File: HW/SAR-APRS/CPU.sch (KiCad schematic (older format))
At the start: 16 parts

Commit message: schematic update
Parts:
- removed J?: USB_B_Micro, symbol Connector:USB_B_Micro
- added C? (x3): 100nF, symbol device:C_Small
- added D? (x2): LED, symbol device:LED
- added J?: USB_B_Mini, symbol Connector:USB_B_Mini
- added R? (x2): 680, symbol device:R_Small
- added R? (x2): 1k, symbol device:R_Small
- added Y?: 16MHz, symbol device:Crystal_Small
- C? (x5): value C_Small -> 100nF
- J?: value HEADER_2x03 -> JTAG
- R?: value R_Small -> 1k
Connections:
- net labels added: BAT_SENS, D11\MOSI, D12\MISO, D13\SCK, GPS_RXD, GPS_TXD, LED, RESET, RFMOD_AUX, RFMOD_PTT, RXD, TXD
- wire segments 72 -> 113
- no-connect marks 1 -> 12
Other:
- moved on the sheet: C?, D?, J?, R?, U?

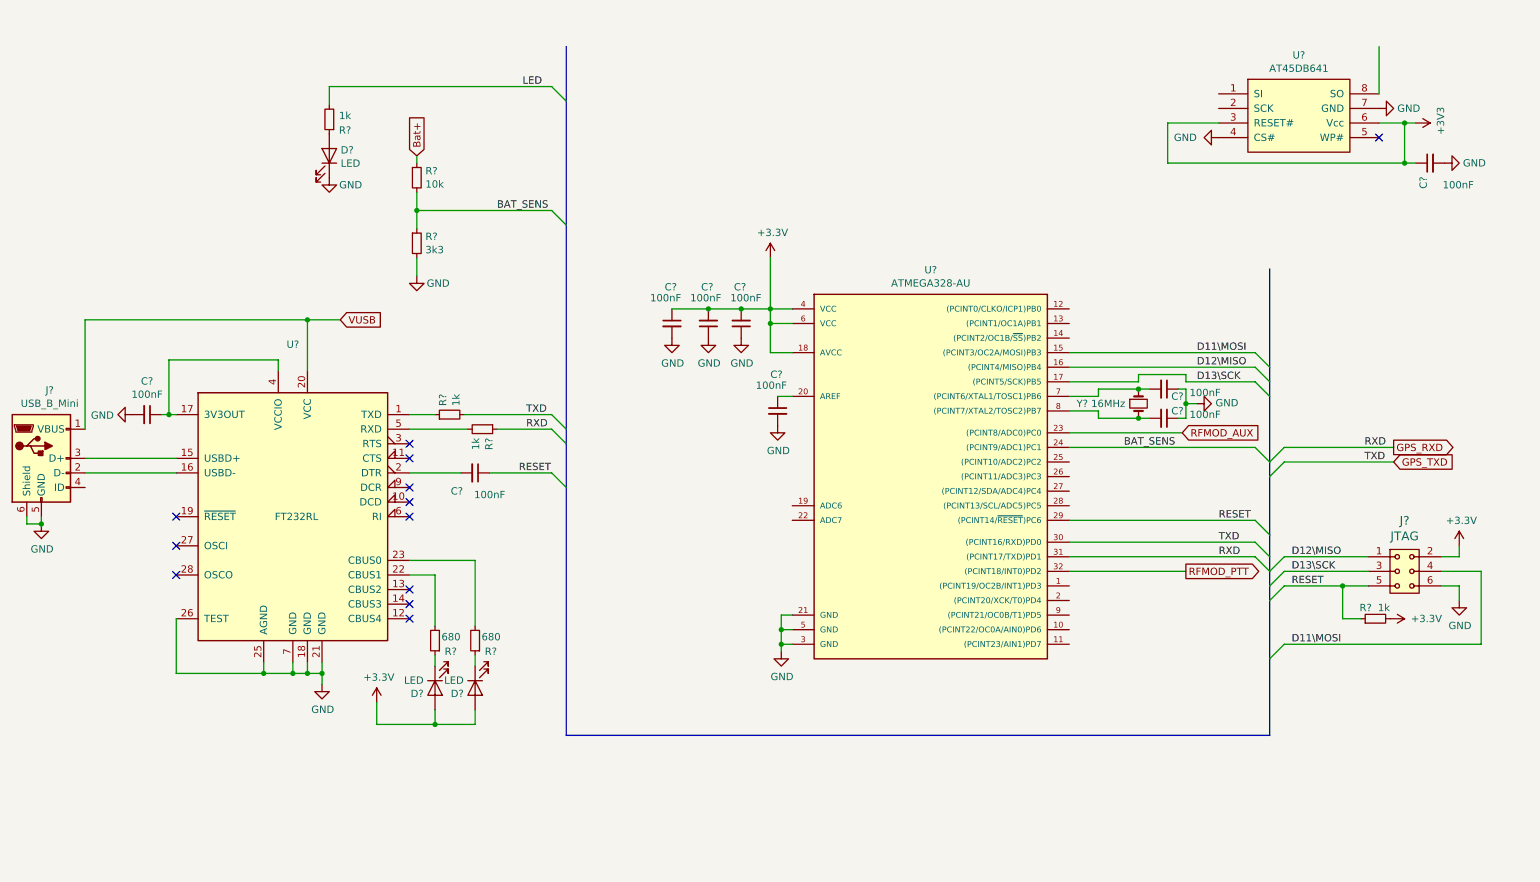
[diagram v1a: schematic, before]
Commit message: schematic update
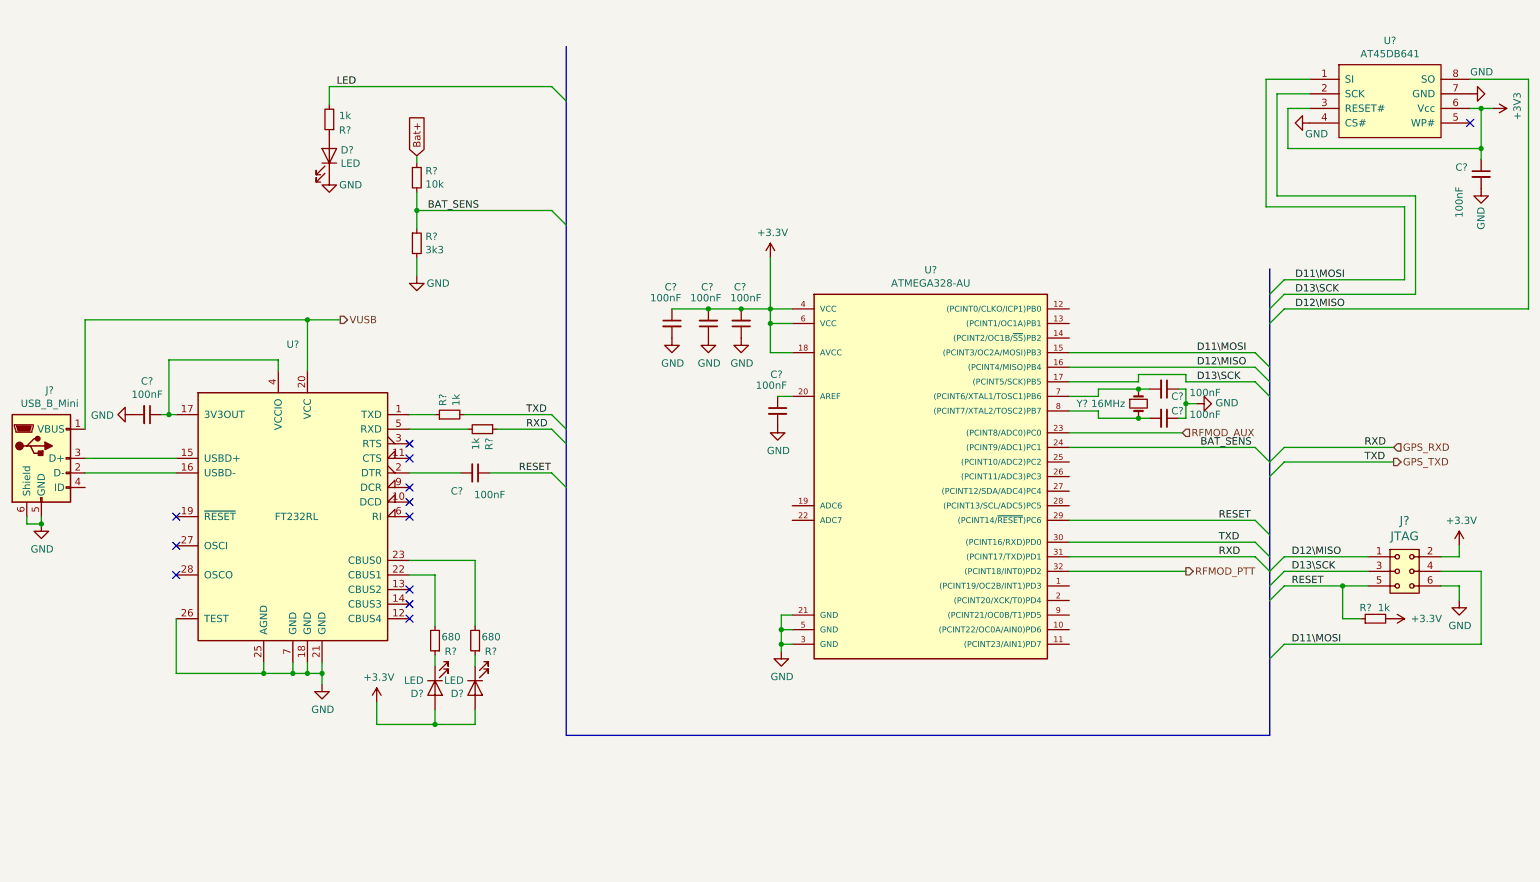
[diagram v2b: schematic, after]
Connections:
- net D11\MOSI: now also U?.1 (SI)
- net D12\MISO: now also U?.8 (SO)
- net D13\SCK: now also U?.2 (SCK)
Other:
- moved on the sheet: C?, U?
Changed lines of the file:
@@
 $Descr A4 11693 8268
 encoding utf-8
-Sheet 5 6
+Sheet 4 6
 Title ""
 Date ""
@@
 L power:GND #PWR?
 U 1 1 5CB8F51A
-P 10050 1225
+P 10675 1125
 AR Path="/5CB8F51A" Ref="#PWR?"  Part="1"
 AR Path="/5CB07977/5CB8F51A" Ref="#PWR?"  Part="1"
-F 0 "#PWR?" H 10050 975 50  0001 C CNN
-F 1 "GND" V 10050 1100 50  0000 R CNN
-F 2 "" H 10050 1225 50  0001 C CNN
-F 3 "" H 10050 1225 50  0001 C CNN
-	1    10050 1225
+F 0 "#PWR?" H 10675 875 50  0001 C CNN
+F 1 "GND" V 10525 1125 50  0000 R CNN
+F 2 "" H 10675 1125 50  0001 C CNN
+F 3 "" H 10675 1125 50  0001 C CNN
+	1    10675 1125
 	0    -1   1    0
 $EndComp
@@
 L power:+3V3 #PWR?
 U 1 1 5CB8F520
-P 10300 1325
+P 10825 1225
 AR Path="/5CB8F520" Ref="#PWR?"  Part="1"
 AR Path="/5CB07977/5CB8F520" Ref="#PWR?"  Part="1"
-F 0 "#PWR?" H 10300 1175 50  0001 C CNN
-F 1 "+3V3" H 10315 1498 50  0000 C CNN
-F 2 "" H 10300 1325 50  0001 C CNN
-F 3 "" H 10300 1325 50  0001 C CNN
-	1    10300 1325
+F 0 "#PWR?" H 10825 1075 50  0001 C CNN
+F 1 "+3V3" H 10840 1398 50  0000 C CNN
+F 2 "" H 10825 1225 50  0001 C CNN
+F 3 "" H 10825 1225 50  0001 C CNN
+	1    10825 1225
 	0    1    -1   0
 $EndComp
@@
 L device:C_Small C?
 U 1 1 5CB8F526
-P 10400 1600
+P 10750 1675
 AR Path="/5CB8F526" Ref="C?"  Part="1"
 AR Path="/5CB07977/5CB8F526" Ref="C?"  Part="1"
-F 0 "C?" H 10492 1646 50  0000 L CNN
-F 1 "100nF" V 10550 1300 50  0000 L CNN
-F 2 "" H 10400 1600 50  0001 C CNN
-F 3 "~" H 10400 1600 50  0001 C CNN
-	1    10400 1600
-	0    -1   1    0
+F 0 "C?" H 10842 1721 50  0000 L CNN
+F 1 "100nF" V 10900 1375 50  0000 L CNN
+F 2 "" H 10750 1675 50  0001 C CNN
+F 3 "~" H 10750 1675 50  0001 C CNN
+	1    10750 1675
+	-1   0    0    -1
 $EndComp
 $Comp
 L power:GND #PWR?
 U 1 1 5CB8F52C
-P 8950 1425
+P 9575 1325
 AR Path="/5CB8F52C" Ref="#PWR?"  Part="1"
 AR Path="/5CB07977/5CB8F52C" Ref="#PWR?"  Part="1"
-F 0 "#PWR?" H 8950 1175 50  0001 C CNN
-F 1 "GND" V 8950 1275 50  0000 R CNN
-F 2 "" H 8950 1425 50  0001 C CNN
-F 3 "" H 8950 1425 50  0001 C CNN
-	1    8950 1425
+F 0 "#PWR?" H 9575 1075 50  0001 C CNN
+F 1 "GND" V 9500 1450 50  0000 R CNN
+F 2 "" H 9575 1325 50  0001 C CNN
+F 3 "" H 9575 1325 50  0001 C CNN
+	1    9575 1325
 	0    1    -1   0
 $EndComp
@@
 L APRS_modules:AT45DB081 U?
 U 1 1 5CB8F532
-P 9500 1275
+P 10125 1175
 AR Path="/5CB8F532" Ref="U?"  Part="1"
 AR Path="/5CB07977/5CB8F532" Ref="U?"  Part="1"
-F 0 "U?" H 9500 1690 50  0000 C CNN
-F 1 "AT45DB641" H 9500 1599 50  0000 C CNN
-F 2 "Mlab_IO:SOIC-8_3.9x4.9mm_Pitch1.27mm" H 8950 1525 50  0001 C CNN
-F 3 "" H 8950 1525 50  0001 C CNN
-	1    9500 1275
-	1    0    0    -1
-$EndComp
-NoConn ~ 10050 1425
-Wire Wire Line
-	10050 1325 10225 1325
-Wire Wire Line
-	10300 1600 10225 1600
-Connection ~ 10225 1325
-Wire Wire Line
-	10225 1325 10300 1325
+F 0 "U?" H 10125 1590 50  0000 C CNN
+F 1 "AT45DB641" H 10125 1499 50  0000 C CNN
+F 2 "Mlab_IO:SOIC-8_3.9x4.9mm_Pitch1.27mm" H 9575 1425 50  0001 C CNN
+F 3 "" H 9575 1425 50  0001 C CNN
+	1    10125 1175
+	1    0    0    -1
+$EndComp
+NoConn ~ 10675 1325
+Wire Wire Line
+	10675 1225 10750 1225
+Wire Wire Line
+	10750 1575 10750 1500
+Connection ~ 10750 1225
+Wire Wire Line
+	10750 1225 10825 1225
 $Comp
 L power:GND #PWR?
 U 1 1 5CB8F53D
-P 10500 1600
+P 10750 1775
 AR Path="/5CB8F53D" Ref="#PWR?"  Part="1"
 AR Path="/5CB07977/5CB8F53D" Ref="#PWR?"  Part="1"
-F 0 "#PWR?" H 10500 1350 50  0001 C CNN
-F 1 "GND" V 10500 1475 50  0000 R CNN
-F 2 "" H 10500 1600 50  0001 C CNN
-F 3 "" H 10500 1600 50  0001 C CNN
-	1    10500 1600
-	0    -1   1    0
-$EndComp
-Wire Wire Line
-	8950 1325 8600 1325
-Wire Wire Line
-	8600 1325 8600 1600
-Wire Wire Line
-	8600 1600 10225 1600
-Connection ~ 10225 1600
-Wire Wire Line
-	10225 1600 10225 1325
-Wire Wire Line
-	10050 800  10050 1125
+F 0 "#PWR?" H 10750 1525 50  0001 C CNN
+F 1 "GND" V 10750 1650 50  0000 R CNN
+F 2 "" H 10750 1775 50  0001 C CNN
+F 3 "" H 10750 1775 50  0001 C CNN
+	1    10750 1775
+	-1   0    0    -1
+$EndComp
+Wire Wire Line
+	9575 1225 9425 1225
+Wire Wire Line
+	9425 1225 9425 1500
+Wire Wire Line
+	9425 1500 10750 1500
+Connection ~ 10750 1500
+Wire Wire Line
+	10750 1500 10750 1225
 $Comp
 L ftdi:FT232RL U?
@@
 Wire Wire Line
 	2700 2675 2700 3025
-Text GLabel 2925 2675 2    50   Input ~ 0
-VUSB
 Wire Wire Line
 	2925 2675 2700 2675
@@
 Wire Wire Line
 	8725 3100 9200 3100
-Text GLabel 8725 4400 2    50   Output ~ 0
-RFMOD_PTT
 Wire Wire Line
 	7925 4400 8725 4400
-Text GLabel 8700 3450 2    50   Input ~ 0
-RFMOD_AUX
 Wire Wire Line
 	7925 3450 8700 3450
@@
 Text Label 4150 3725 0    50   ~ 0
 RESET
-Text Label 4000 1925 0    50   ~ 0
+Text Label 3525 1925 0    50   ~ 0
 BAT_SENS
-Text Label 8300 3550 0    50   ~ 0
+Text Label 8825 3550 0    50   ~ 0
 BAT_SENS
 Entry Wire Line
@@
 Wire Wire Line
 	9400 3650 10150 3650
+Text Label 9950 3650 0    50   ~ 0
+TXD
+Text Label 9950 3550 0    50   ~ 0
+RXD
+Text Label 2900 1075 0    50   ~ 0
+LED
+Text HLabel 10150 3550 2    50   Input ~ 0
+GPS_RXD
+Text HLabel 10150 3650 2    50   Output ~ 0
+GPS_TXD
+Text HLabel 8725 4400 2    50   Output ~ 0
+RFMOD_PTT
+Text HLabel 8700 3450 2    50   Input ~ 0
+RFMOD_AUX
+Wire Wire Line
+	10675 1025 11075 1025
+Entry Wire Line
+	9300 2500 9400 2400
+Entry Wire Line
+	9300 2600 9400 2500
+Entry Wire Line
+	9300 2700 9400 2600
+Wire Wire Line
+	9400 2600 11075 2600
+Wire Wire Line
+	11075 1025 11075 2600
+Wire Wire Line
+	9350 1125 9350 1825
+Wire Wire Line
+	9350 1825 10300 1825
+Wire Wire Line
+	10300 1825 10300 2500
+Wire Wire Line
+	10300 2500 9400 2500
+Wire Wire Line
+	9350 1125 9575 1125
+Wire Wire Line
+	9575 1025 9275 1025
+Wire Wire Line
+	9275 1025 9275 1900
+Wire Wire Line
+	9275 1900 10225 1900
+Wire Wire Line
+	10225 1900 10225 2400
+Wire Wire Line
+	10225 2400 9400 2400
 Wire Bus Line
 	4475 800  4475 5525
 Wire Bus Line
 	9300 2325 9300 5525
-Text GLabel 10150 3550 2    50   Output ~ 0
-GPS_RXD
-Text GLabel 10150 3650 2    50   Input ~ 0
-GPS_TXD
-Text Label 9950 3650 0    50   ~ 0
-TXD
-Text Label 9950 3550 0    50   ~ 0
-RXD
-Text Label 4175 1075 0    50   ~ 0
-LED
+Text Label 9475 2400 0    50   ~ 0
+D11\MOSI
+Text Label 9475 2600 0    50   ~ 0
+D12\MISO
+Text Label 9475 2500 0    50   ~ 0
+D13\SCK
+Text HLabel 2925 2675 2    50   Output ~ 0
+VUSB
 $EndSCHEMATC

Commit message: schem and pcb update
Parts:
- removed D? (x2): LED, symbol device:LED
- removed R? (x2): 680, symbol device:R_Small
- removed R? (x2): 1k, symbol device:R_Small
- removed U?: FT232RL, Housings_SSOP:SSOP-28_5.3x10.2mm_Pitch0.65mm, symbol ftdi:FT232RL
- added C27: 100nF, symbol device:C_Small
- added J5: HEADER_1x04, symbol MLAB_HEADER:HEADER_1x04
- added U7: CH340C, IO:SOP-16_4.55x10.3mm_P1.27mm, symbol CH34xx:CH340G
- C17, C20: renamed from C?; value 100nF -> 22pF
- gave numbers to parts that had none: 17
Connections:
- net +3V3: now also C27.1, J5.3, U7.4 (V3)
- net GND: now also C27.2, J5.4, U7.1 (GND)
- net RFMOD_PTT: now also U6.9 ((PCINT21/OC0B/T1)PD5); no longer U6.32 ((PCINT18/INT0)PD2)
- net VUSB: now also C19.1, U7.16 (VCC)
- net at J2.2 (D-): now also U7.6 (D-)
- net at J2.3 (D+): now also U7.5 (D+)
- net at C21.2: now also U7.13 (DTR)
- net RFMOD_RXD: now reaches U6.1 ((PCINT19/OC2B/INT1)PD3)
- net BT_TXD: now reaches U6.10 ((PCINT22/OC0A/AIN0)PD6)
- net BT_RXD: now reaches U6.11 ((PCINT23/AIN1)PD7)
- net BT_LED2: now reaches U6.12 ((PCINT0/CLKO/ICP1)PB0)
- net BT_CMD: now reaches U6.13 ((PCINT1/OC1A)PB1)
- net GPS_PPS: now reaches U6.14 ((PCINT2/OC1B/~SS~)PB2)
- net RFMOD_MIC: now reaches U6.2 ((PCINT20/XCK/T0)PD4)
- net OLED_SDA: now reaches U6.25 ((PCINT10/ADC2)PC2)
- net OLED_SDA: now also J5.1
- net OLED_SCL: now reaches U6.26 ((PCINT11/ADC3)PC3)
- net OLED_SCL: now also J5.2
- new net RFMOD_TXD: U6.32 ((PCINT18/INT0)PD2)
- new net RXD: U7.3 (RX)
- new net TXD: U7.2 (TX)
- no-connect marks 12 -> 9
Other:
- note added: "OLED DISPLAY"
- moved on the sheet: C19, C21, J2, Y1

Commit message: schm and pcb update
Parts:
- C13, C14, C15, C16, C17, C18, C19, C20, C21, C27: footprint (none) -> Capacitors_SMD:C_0603
- D4: renamed from D3; footprint (none) -> LEDs:LED_0603
- J2: footprint (none) -> Connectors:USB_Mini-B
- R15, R16, R17, R20: footprint (none) -> Resistors_SMD:R_0603
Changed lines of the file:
@@
 P 2850 1550
 AR Path="/5CB7F360" Ref="D?"  Part="1"
-AR Path="/5CB07977/5CB7F360" Ref="D3"  Part="1"
-F 0 "D3" V 2889 1628 50  0000 L CNN
+AR Path="/5CB07977/5CB7F360" Ref="D4"  Part="1"
+F 0 "D4" V 2889 1628 50  0000 L CNN
 F 1 "LED" V 2798 1628 50  0000 L CNN
-F 2 "" H 2850 1550 50  0001 C CNN
+F 2 "LEDs:LED_0603" H 2850 1550 50  0001 C CNN
 F 3 "~" H 2850 1550 50  0001 C CNN
 	1    2850 1550
@@
 F 0 "R15" H 2650 1350 50  0000 L CNN
 F 1 "1k" H 2700 1275 50  0000 L CNN
-F 2 "" H 2850 1300 50  0001 C CNN
+F 2 "Resistors_SMD:R_0603" H 2850 1300 50  0001 C CNN
 F 3 "~" H 2850 1300 50  0001 C CNN
 	1    2850 1300
@@
 F 0 "R16" H 3509 1746 50  0000 L CNN
 F 1 "10k" H 3509 1655 50  0000 L CNN
-F 2 "" H 3450 1700 50  0001 C CNN
+F 2 "Resistors_SMD:R_0603" H 3450 1700 50  0001 C CNN
 F 3 "~" H 3450 1700 50  0001 C CNN
 	1    3450 1700
@@
 F 0 "R17" H 3509 2196 50  0000 L CNN
 F 1 "3k3" H 3509 2105 50  0000 L CNN
-F 2 "" H 3450 2150 50  0001 C CNN
+F 2 "Resistors_SMD:R_0603" H 3450 2150 50  0001 C CNN
 F 3 "~" H 3450 2150 50  0001 C CNN
 	1    3450 2150
@@
 F 0 "C13" H 10842 1721 50  0000 L CNN
 F 1 "100nF" V 10900 1375 50  0000 L CNN
-F 2 "" H 10750 1675 50  0001 C CNN
+F 2 "Capacitors_SMD:C_0603" H 10750 1675 50  0001 C CNN
 F 3 "~" H 10750 1675 50  0001 C CNN
 	1    10750 1675
@@
 F 0 "C19" V 975 3225 50  0000 C CNN
 F 1 "100nF" V 987 3425 50  0000 C CNN
-F 2 "" H 1125 3425 50  0001 C CNN
+F 2 "Capacitors_SMD:C_0603" H 1125 3425 50  0001 C CNN
 F 3 "~" H 1125 3425 50  0001 C CNN
 	1    1125 3425
@@
 F 0 "C21" V 3375 3775 50  0000 C CNN
 F 1 "100nF" V 3400 4000 50  0000 C CNN
-F 2 "" H 3250 3900 50  0001 C CNN
+F 2 "Capacitors_SMD:C_0603" H 3250 3900 50  0001 C CNN
 F 3 "~" H 3250 3900 50  0001 C CNN
 	1    3250 3900
@@
 F 0 "R20" V 10100 4750 50  0000 L CNN
 F 1 "1k" V 10100 4625 50  0000 L CNN
-F 2 "" H 10025 4725 50  0001 C CNN
+F 2 "Resistors_SMD:R_0603" H 10025 4725 50  0001 C CNN
 F 3 "~" H 10025 4725 50  0001 C CNN
 	1    10025 4725
@@
 F 0 "C15" H 5500 2450 50  0000 R CNN
 F 1 "100nF" H 5575 2525 50  0000 R CNN
-F 2 "" H 5450 2700 50  0001 C CNN
+F 2 "Capacitors_SMD:C_0603" H 5450 2700 50  0001 C CNN
 F 3 "~" H 5450 2700 50  0001 C CNN
 	1    5450 2700
@@
 F 0 "C16" H 5725 2450 50  0000 R CNN
 F 1 "100nF" H 5750 2525 50  0000 R CNN
-F 2 "" H 5675 2700 50  0001 C CNN
+F 2 "Capacitors_SMD:C_0603" H 5675 2700 50  0001 C CNN
 F 3 "~" H 5675 2700 50  0001 C CNN
 	1    5675 2700
@@
 F 0 "C14" H 5150 2950 50  0000 L CNN
 F 1 "100nF" H 5050 2875 50  0000 L CNN
-F 2 "" H 5200 2700 50  0001 C CNN
+F 2 "Capacitors_SMD:C_0603" H 5200 2700 50  0001 C CNN
 F 3 "~" H 5200 2700 50  0001 C CNN
 	1    5200 2700
@@
 F 0 "J2" H 982 4467 50  0000 C CNN
 F 1 "USB_B_Mini" H 982 4376 50  0000 C CNN
-F 2 "" H 1075 3950 50  0001 C CNN
+F 2 "Connectors:USB_Mini-B" H 1075 3950 50  0001 C CNN
 F 3 "~" H 1075 3950 50  0001 C CNN
 	1    925  4000
@@
 F 0 "C18" H 5875 3550 50  0000 L CNN
 F 1 "100nF" H 5775 3475 50  0000 L CNN
-F 2 "" H 5925 3300 50  0001 C CNN
+F 2 "Capacitors_SMD:C_0603" H 5925 3300 50  0001 C CNN
 F 3 "~" H 5925 3300 50  0001 C CNN
 	1    5925 3300
@@
 F 0 "C20" V 8625 3150 50  0000 L CNN
 F 1 "22pF" V 8625 3400 50  0000 L CNN
-F 2 "" H 8575 3350 50  0001 C CNN
+F 2 "Capacitors_SMD:C_0603" H 8575 3350 50  0001 C CNN
 F 3 "~" H 8575 3350 50  0001 C CNN
 	1    8575 3350
@@
 F 0 "C17" V 8525 2975 50  0000 L CNN
 F 1 "22pF" V 8525 3175 50  0000 L CNN
-F 2 "" H 8575 3150 50  0001 C CNN
+F 2 "Capacitors_SMD:C_0603" H 8575 3150 50  0001 C CNN
 F 3 "~" H 8575 3150 50  0001 C CNN
 	1    8575 3150
@@
 F 0 "C27" V 975 2900 50  0000 C CNN
 F 1 "100nF" V 975 3075 50  0000 C CNN
-F 2 "" H 1125 3075 50  0001 C CNN
+F 2 "Capacitors_SMD:C_0603" H 1125 3075 50  0001 C CNN
 F 3 "~" H 1125 3075 50  0001 C CNN
 	1    1125 3075

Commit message: PCB update
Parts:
- removed Y1: 16MHz, symbol device:Crystal_Small
- added R18: 2K, Resistors_SMD:R_0805, symbol device:R_Small
- added R19: 330, Resistors_SMD:R_0805, symbol device:R_Small
- added R21: 620, Resistors_SMD:R_0805, symbol device:R_Small
- added SW1, SW2, SW3: SW_DPST_x2, Buttons_Switches_SMD:SW_SPST_EVQP0, symbol Switch:SW_DPST_x2
- added Y1: 16MHz, Mlab_XTAL:ISM81, symbol device:Crystal_GND24_Small
- C13, C14, C15, C16, C17, C18, C19, C20, C21, C27: footprint Capacitors_SMD:C_0603 -> Capacitors_SMD:C_0805
- D4: footprint LEDs:LED_0603 -> LEDs:LED_0805
- J3: footprint (none) -> Mlab_Pin_Headers:Straight_2x03
- J5: footprint (none) -> Mlab_Pin_Headers:Straight_1x04
- R15, R16, R17, R20: footprint Resistors_SMD:R_0603 -> Resistors_SMD:R_0805
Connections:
- net RXD is gone; now on net GPS_RXD: U7.3 (RX)
- net TXD is gone; now on net GPS_TXD: U7.2 (TX)
- net +3V3: now also R18.1
- net GND: now also SW1.1 (A), SW2.1 (A), SW3.1 (A), Y1.2, Y1.4
- net LED: now also U6.28 ((PCINT13/SCL/ADC5)PC5)
- net OLED_SCL: now also U6.25 ((PCINT10/ADC2)PC2); no longer U6.26 ((PCINT11/ADC3)PC3)
- net OLED_SDA: now also U6.26 ((PCINT11/ADC3)PC3); no longer U6.25 ((PCINT10/ADC2)PC2)
- net RFMOD_RXD: now also U6.32 ((PCINT18/INT0)PD2); no longer U6.1 ((PCINT19/OC2B/INT1)PD3)
- net RFMOD_TXD: now also U6.1 ((PCINT19/OC2B/INT1)PD3); no longer U6.32 ((PCINT18/INT0)PD2)
- net at C17.2, U6.7 ((PCINT6/XTAL1/TOSC1)PB6): now also Y1.1
- net at C20.2, U6.8 ((PCINT7/XTAL2/TOSC2)PB7): now also Y1.3
- net BUTTON: now reaches U6.27 ((PCINT12/SDA/ADC4)PC4)
- net BUTTON: now also R18.2, R19.1, SW3.2 (B)
- new net: R19.2, R21.1, SW2.2 (B)
- new net: R21.2, SW1.2 (B)
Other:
- note added: "footprint ok"
